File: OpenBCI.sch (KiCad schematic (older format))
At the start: 46 parts, among them J1 CONN_01X08, J1 MicroSD, J2 CONN_01X02, U1 ADXL345, U3 LM2664, U4 TLV700xx, U5 LP5907, U6 ADS1299

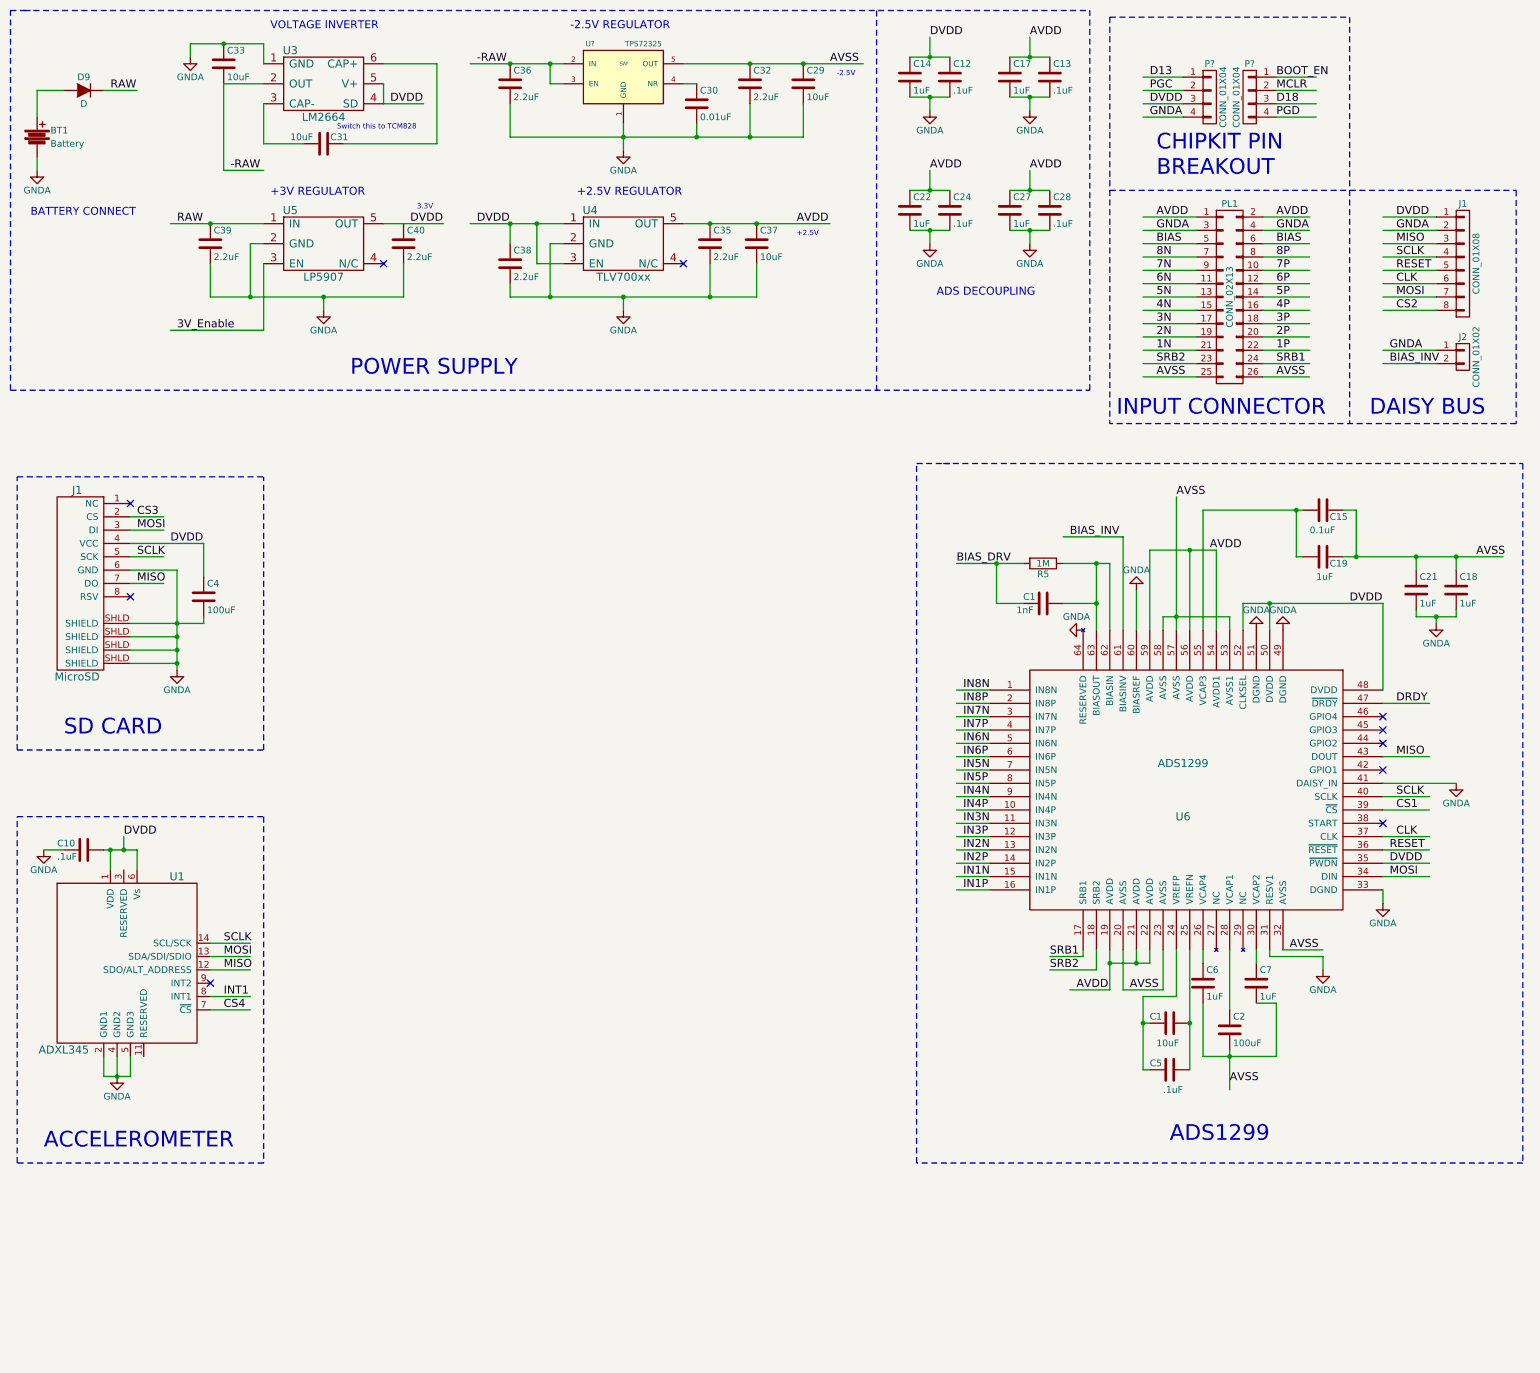
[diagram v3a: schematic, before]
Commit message: + Input filtering block and library components
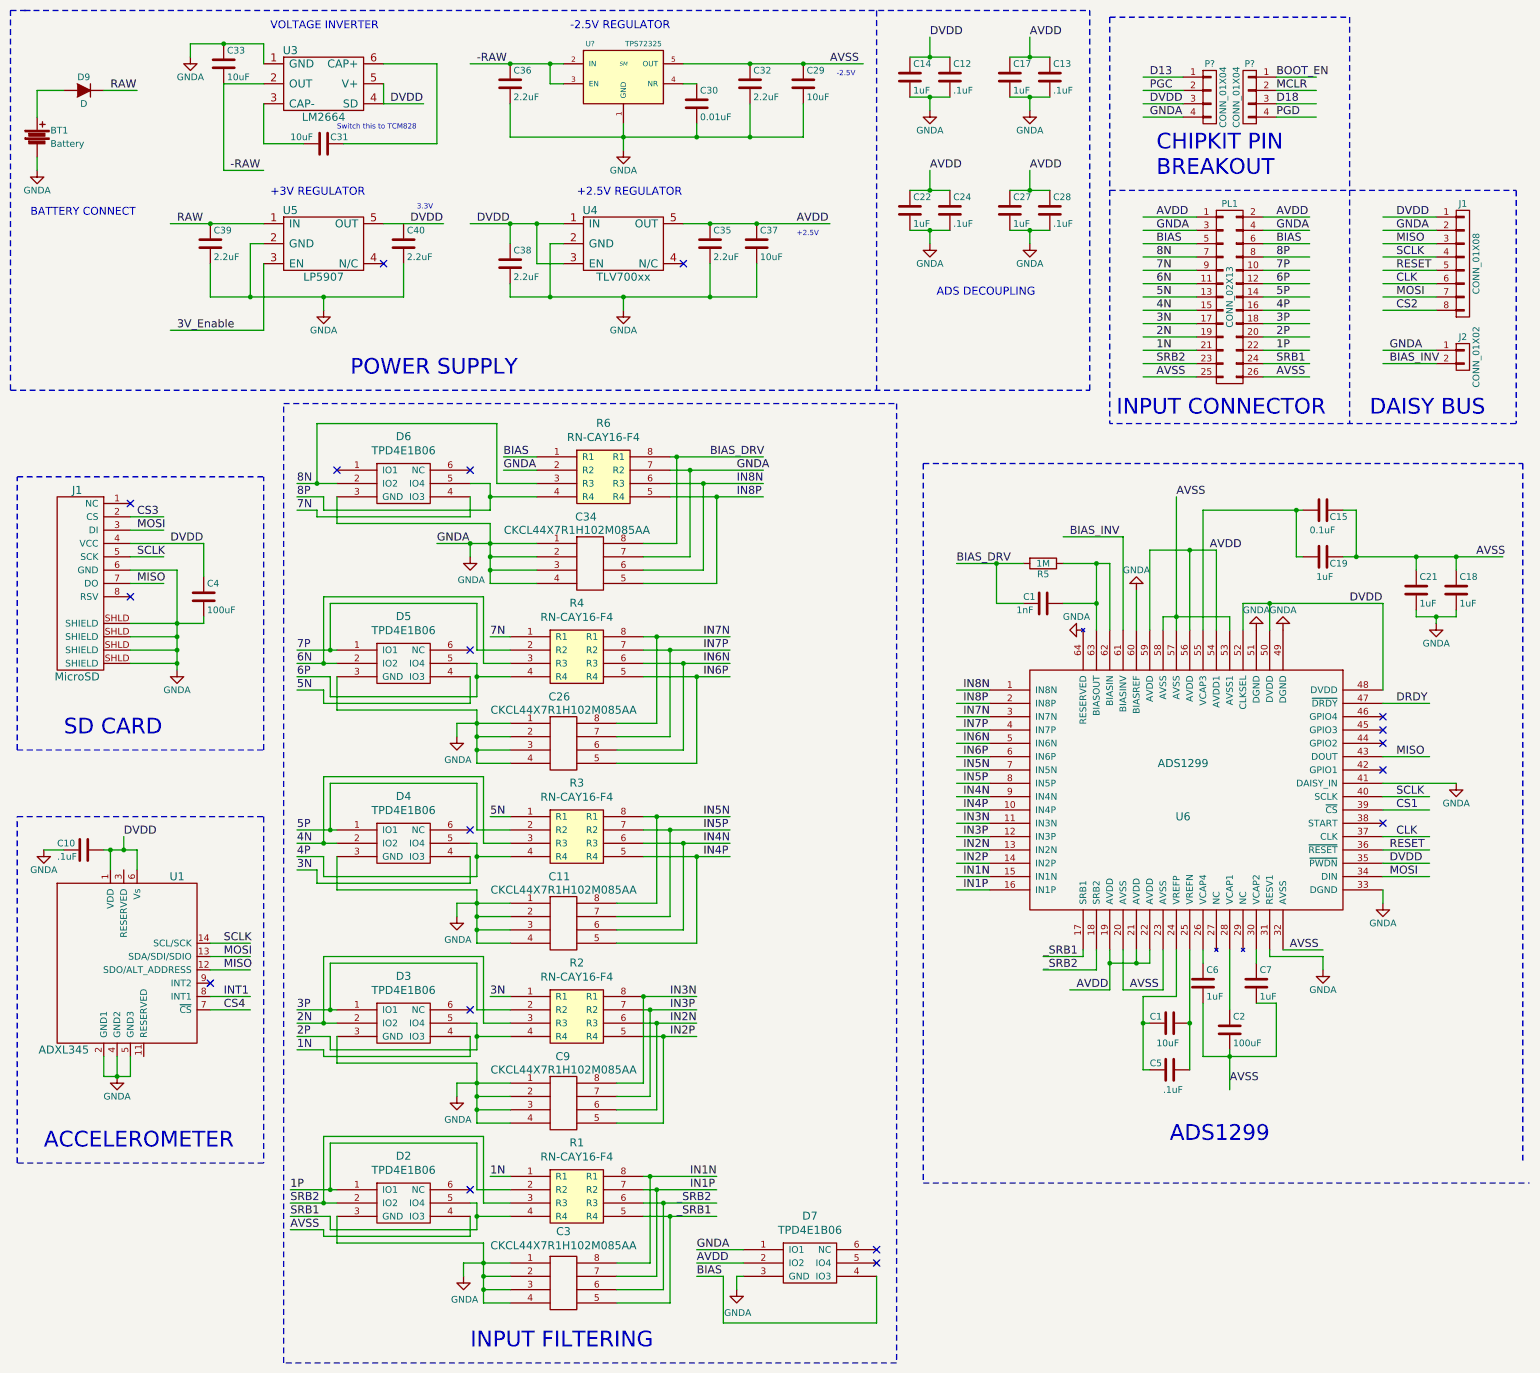
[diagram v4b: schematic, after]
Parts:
- added C11, C26, C3, C34, C9: CKCL44X7R1H102M085AA, symbol CKCL44X7R1H102M085AA
- added D2, D3, D4, D5, D6, D7: TPD4E1B06, symbol TPD4E1B06
- added R1, R2, R3, R4, R6: RN-CAY16-F4, symbol RN-CAY16-F4
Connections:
- net labels added: _SRB1, _SRB2
- wire segments 229 -> 438
- no-connect marks 10 -> 18
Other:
- note added: "INPUT FILTERING"
